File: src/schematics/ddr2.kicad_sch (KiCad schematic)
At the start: 23 parts

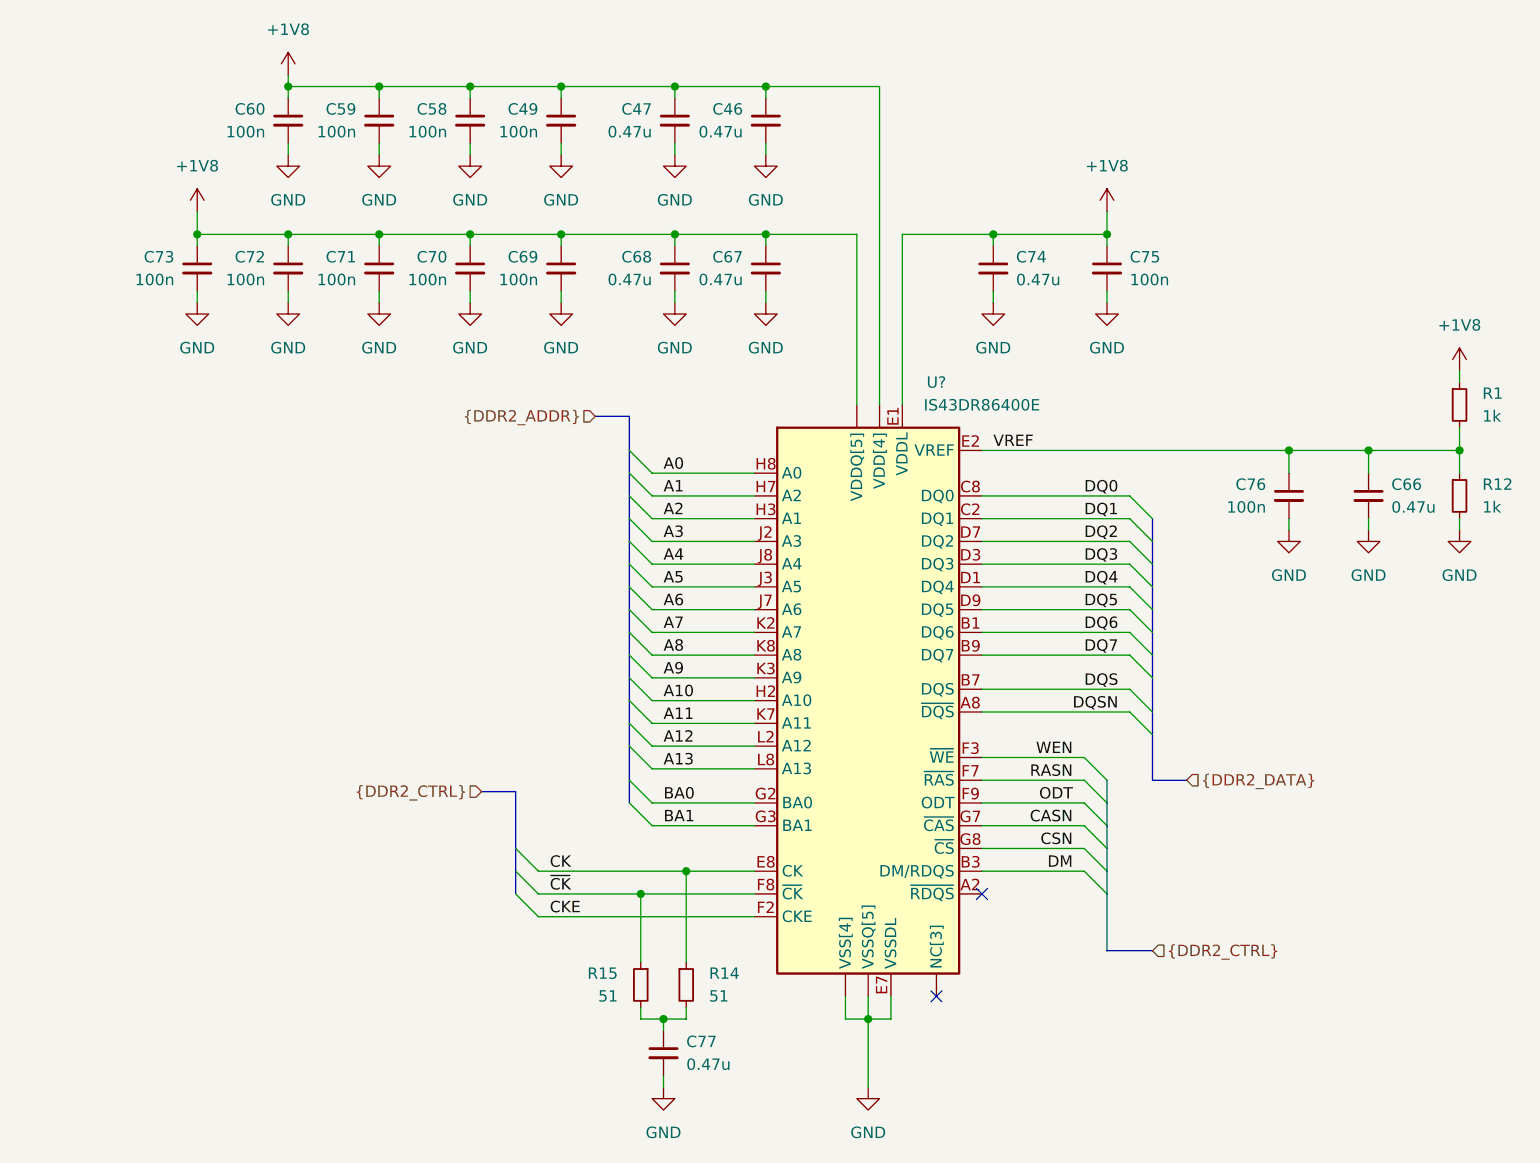
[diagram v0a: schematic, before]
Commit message: Adds the clock oscillator
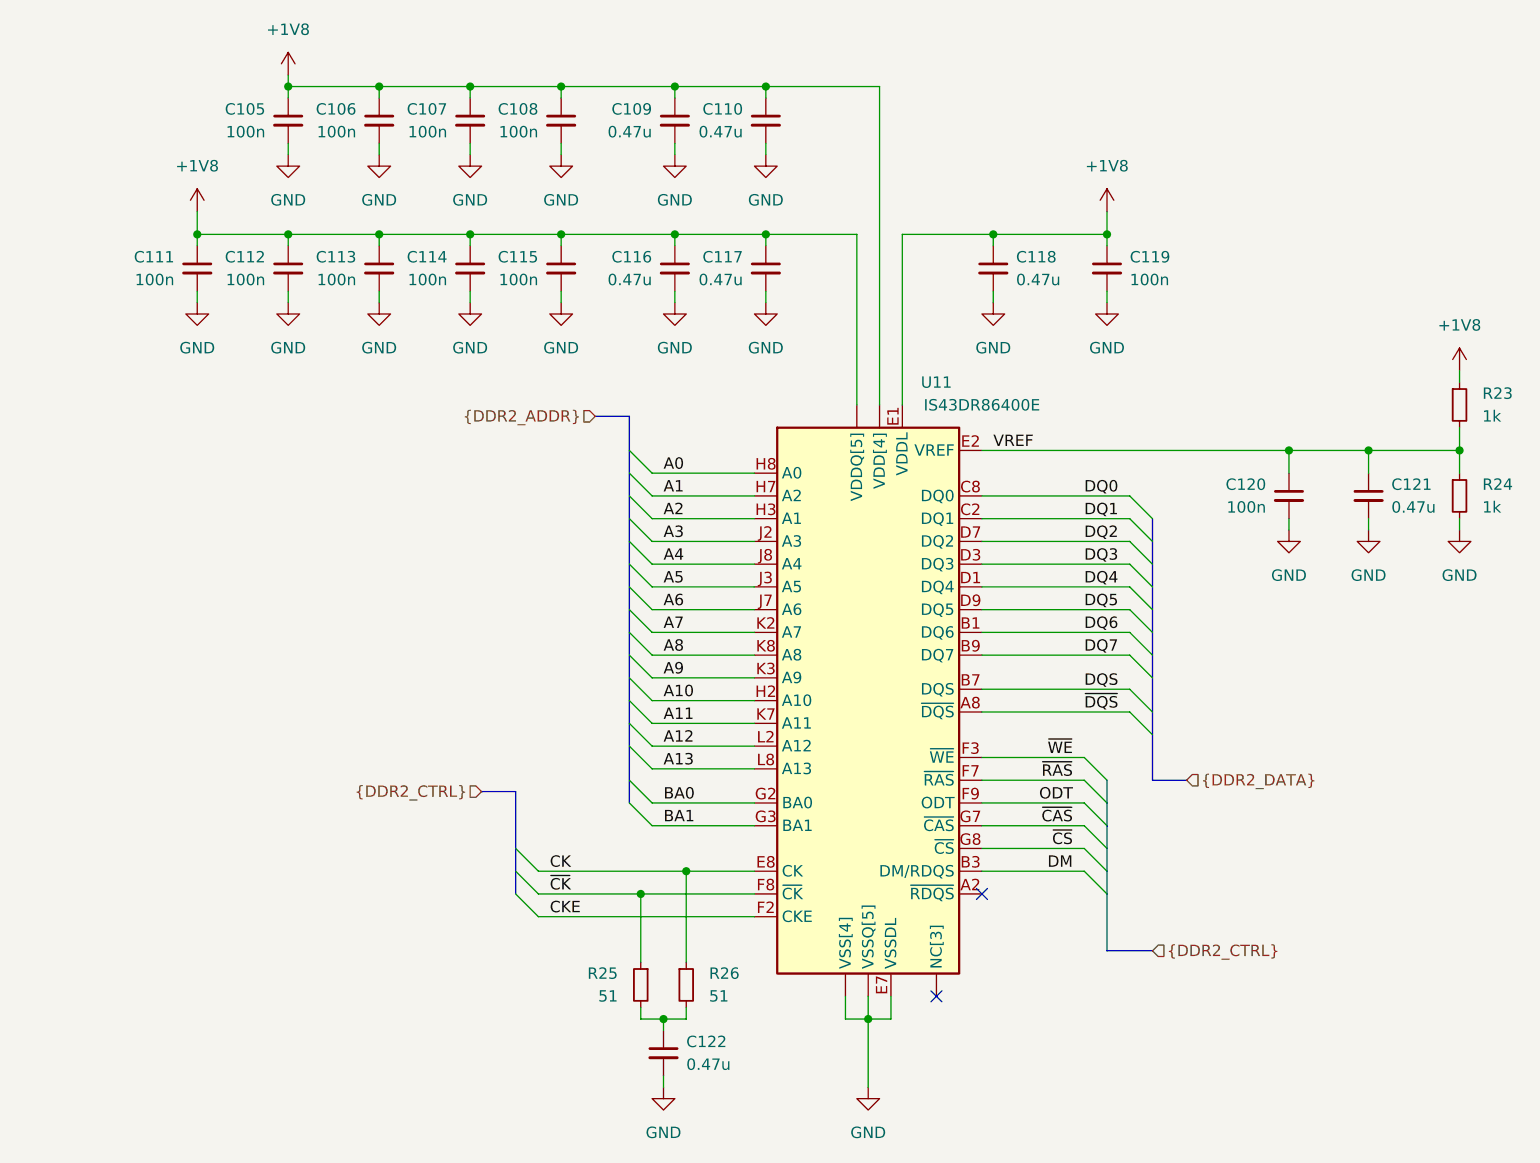
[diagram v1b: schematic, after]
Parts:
- gave numbers to parts that had none: 1
- renumbered C60 to C105, C59 to C106, C58 to C107, C49 to C108, C47 to C109, C46 to C110, C73 to C111, C72 to C112, C71 to C113, C70 to C114, C69 to C115, C68 to C116, C67 to C117, C74 to C118, C75 to C119, C76 to C120, C66 to C121, C77 to C122, R1 to R23, R12 to R24, R15 to R25, R14 to R26
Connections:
- net CASN renamed ~{CAS}
- net CSN renamed ~{CS}
- net DQSN renamed ~{DQS}
- net RASN renamed ~{RAS}
- net WEN renamed ~{WE}

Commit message: Adds bus aliases
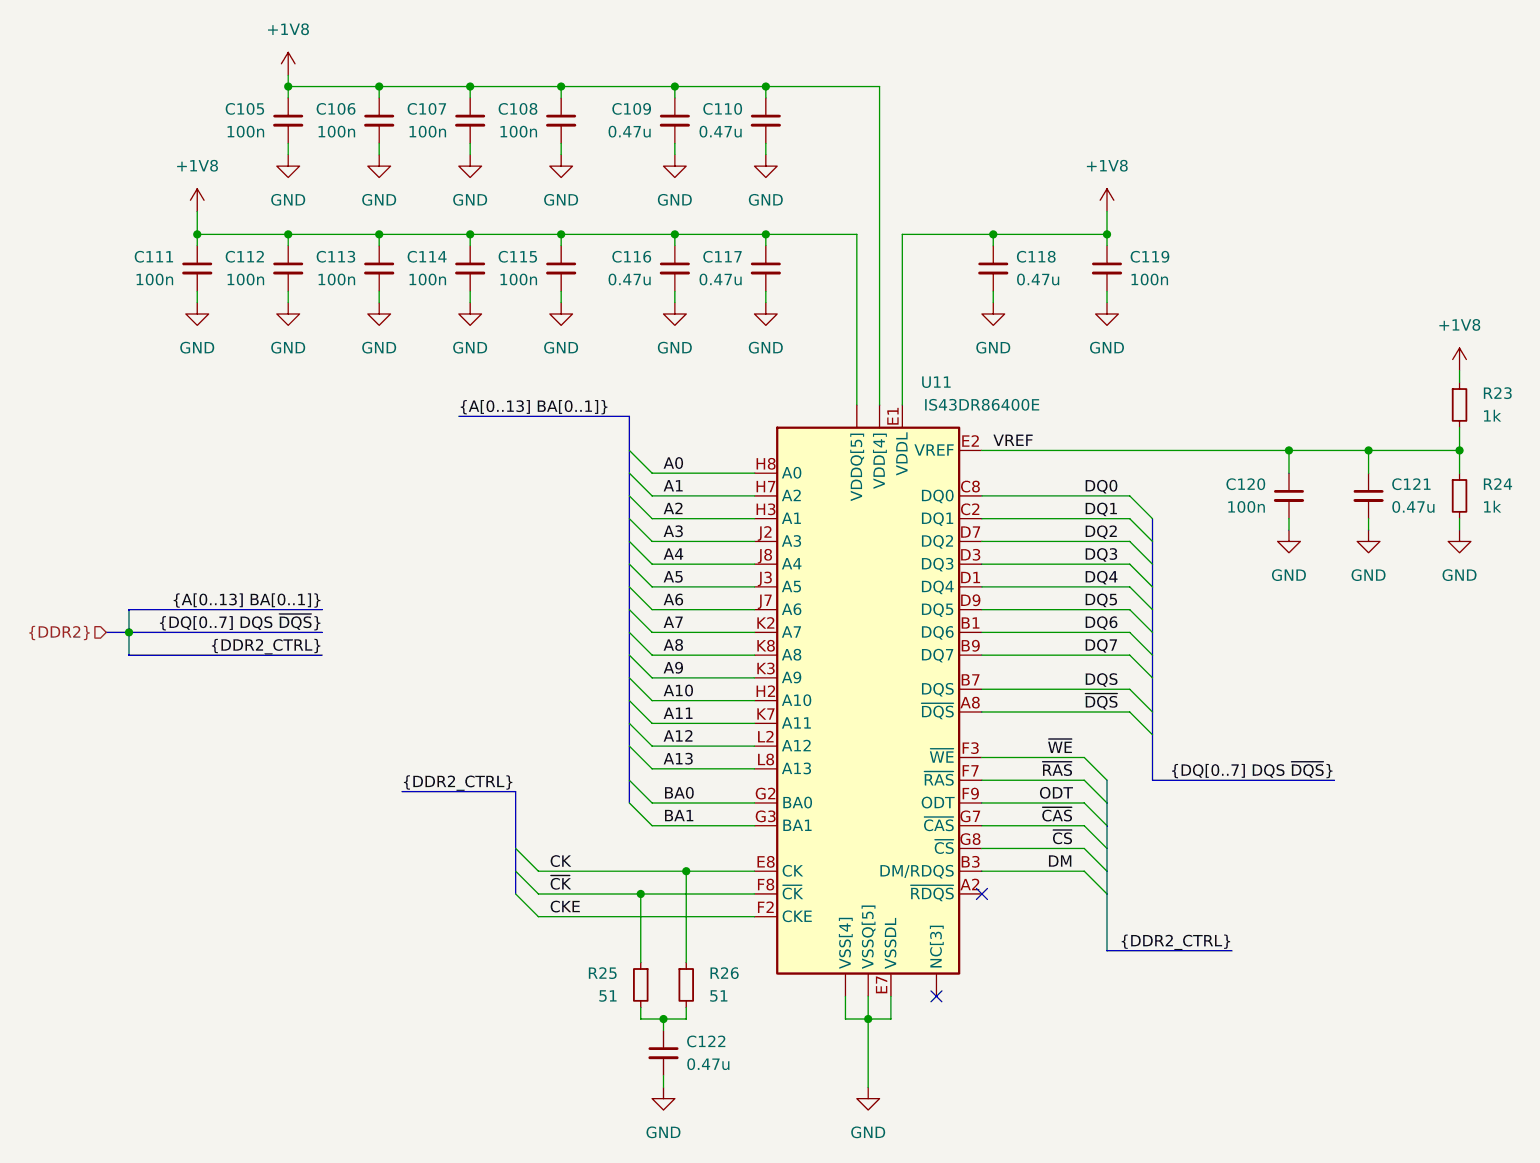
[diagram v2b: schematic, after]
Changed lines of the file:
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@@
 		(rev "${Revision}")
 		(comment 1 "${Project Title}")
-		(comment 2 "SRAM")
+		(comment 2 "DDR2")
 		(comment 3 "${Part Number}")
+	)
+	(bus_alias "DDR2"
+		(members "A[0..13]" "BA[0..1]" "DQ[0..7]" "DQS" "~{DQS}" "{DDR2_CTRL}")
+	)
+	(bus_alias "DDR2_CTRL"
+		(members "~{LB}" "~{UB}" "~{WE}" "~{OE}" "~{CE}")
 	)
 	(junction
@@
 	)
 	(junction
+		(at 67.31 92.71)
+		(diameter 0)
+		(color 0 0 0 0)
+	)
+	(junction
 		(at 129.54 119.38)
 		(diameter 0)
@@
 		)
 	)
+	(bus
+		(pts
+			(xy 104.14 68.58) (xy 123.19 68.58)
+		)
+		(stroke
+			(width 0)
+			(type default)
+		)
+	)
 	(wire
 		(pts
@@
 		)
 	)
+	(bus
+		(pts
+			(xy 67.31 92.71) (xy 88.9 92.71)
+		)
+		(stroke
+			(width 0)
+			(type default)
+		)
+	)
 	(wire
 		(pts
@@
 		)
 	)
+	(bus
+		(pts
+			(xy 97.79 110.49) (xy 110.49 110.49)
+		)
+		(stroke
+			(width 0)
+			(type default)
+		)
+	)
 	(wire
 		(pts
@@
 	(bus
 		(pts
+			(xy 67.31 92.71) (xy 67.31 95.25)
+		)
+		(stroke
+			(width 0)
+			(type default)
+		)
+	)
+	(bus
+		(pts
 			(xy 123.19 105.41) (xy 123.19 102.87)
 		)
@@
 		)
 	)
+	(bus
+		(pts
+			(xy 67.31 92.71) (xy 67.31 90.17)
+		)
+		(stroke
+			(width 0)
+			(type default)
+		)
+	)
 	(wire
 		(pts
@@
 	(bus
 		(pts
-			(xy 181.61 128.27) (xy 176.53 128.27)
-		)
-		(stroke
-			(width 0)
-			(type default)
-		)
-	)
-	(bus
-		(pts
 			(xy 176.53 114.3) (xy 176.53 111.76)
 		)
@@
 	(bus
 		(pts
+			(xy 176.53 128.27) (xy 190.5 128.27)
+		)
+		(stroke
+			(width 0)
+			(type default)
+		)
+	)
+	(bus
+		(pts
 			(xy 123.19 68.58) (xy 123.19 72.39)
 		)
@@
 		)
 	)
+	(bus
+		(pts
+			(xy 64.77 92.71) (xy 67.31 92.71)
+		)
+		(stroke
+			(width 0)
+			(type default)
+		)
+	)
 	(wire
 		(pts
@@
 		)
 	)
+	(bus
+		(pts
+			(xy 67.31 90.17) (xy 88.9 90.17)
+		)
+		(stroke
+			(width 0)
+			(type default)
+		)
+	)
 	(wire
 		(pts
@@
 	(bus
 		(pts
+			(xy 181.61 109.22) (xy 201.93 109.22)
+		)
+		(stroke
+			(width 0)
+			(type default)
+		)
+	)
+	(bus
+		(pts
 			(xy 176.53 128.27) (xy 176.53 121.92)
 		)
@@
 	(bus
 		(pts
+			(xy 88.9 95.25) (xy 67.31 95.25)
+		)
+		(stroke
+			(width 0)
+			(type default)
+		)
+	)
+	(bus
+		(pts
 			(xy 181.61 82.55) (xy 181.61 80.01)
 		)
@@
 		)
 	)
-	(bus
-		(pts
-			(xy 119.38 68.58) (xy 123.19 68.58)
-		)
-		(stroke
-			(width 0)
-			(type default)
-		)
-	)
 	(wire
 		(pts
@@
 		)
 	)
-	(bus
-		(pts
-			(xy 185.42 109.22) (xy 181.61 109.22)
-		)
-		(stroke
-			(width 0)
-			(type default)
-		)
-	)
 	(wire
 		(pts
@@
 	(bus
 		(pts
-			(xy 106.68 110.49) (xy 110.49 110.49)
-		)
-		(stroke
-			(width 0)
-			(type default)
-		)
-	)
-	(bus
-		(pts
 			(xy 123.19 109.22) (xy 123.19 105.41)
 		)
@@
 			(width 0)
 			(type default)
+		)
+	)
+	(label "{DDR2_CTRL}"
+		(at 88.9 95.25 180)
+		(fields_autoplaced yes)
+		(effects
+			(font
+				(size 1.27 1.27)
+			)
+			(justify right bottom)
 		)
 	)
@@
 		)
 	)
+	(label "{A[0..13] BA[0..1]}"
+		(at 88.9 90.17 180)
+		(fields_autoplaced yes)
+		(effects
+			(font
+				(size 1.27 1.27)
+			)
+			(justify right bottom)
+		)
+	)
 	(label "DQS"
 		(at 177.8 99.06 180)
@@
 		)
 	)
+	(label "{DDR2_CTRL}"
+		(at 190.5 128.27 180)
+		(fields_autoplaced yes)
+		(effects
+			(font
+				(size 1.27 1.27)
+			)
+			(justify right bottom)
+		)
+	)
 	(label "DM"
 		(at 172.72 119.38 180)
@@
 		)
 	)
+	(label "{DQ[0..7] DQS ~{DQS}}"
+		(at 88.9 92.71 180)
+		(fields_autoplaced yes)
+		(effects
+			(font
+				(size 1.27 1.27)
+			)
+			(justify right bottom)
+		)
+	)
 	(label "A0"
 		(at 127 74.93 0)
@@
 		)
 	)
+	(label "{DQ[0..7] DQS ~{DQS}}"
+		(at 201.93 109.22 180)
+		(fields_autoplaced yes)
+		(effects
+			(font
+				(size 1.27 1.27)
+			)
+			(justify right bottom)
+		)
+	)
 	(label "ODT"
 		(at 172.72 111.76 180)
@@
 		)
 	)
+	(label "{DDR2_CTRL}"
+		(at 97.79 110.49 0)
+		(fields_autoplaced yes)
+		(effects
+			(font
+				(size 1.27 1.27)
+			)
+			(justify left bottom)
+		)
+	)
+	(label "{A[0..13] BA[0..1]}"
+		(at 104.14 68.58 0)
+		(fields_autoplaced yes)
+		(effects
+			(font
+				(size 1.27 1.27)
+			)
+			(justify left bottom)
+		)
+	)
 	(label "A1"
 		(at 127 77.47 0)
@@
 		)
 	)
-	(hierarchical_label "{DDR2_CTRL}"
+	(hierarchical_label "{DDR2}"
 		(shape input)
-		(at 181.61 128.27 0)
-		(fields_autoplaced yes)
-		(effects
-			(font
-				(size 1.27 1.27)
-			)
-			(justify left)
-		)
-	)
-	(hierarchical_label "{DDR2_CTRL}"
-		(shape input)
-		(at 106.68 110.49 180)
+		(at 64.77 92.71 180)
 		(fields_autoplaced yes)
 		(effects
@@
 		)
 	)
-	(hierarchical_label "{DDR2_ADDR}"
-		(shape input)
-		(at 119.38 68.58 180)
-		(fields_autoplaced yes)
-		(effects
-			(font
-				(size 1.27 1.27)
-			)
-			(justify right)
-		)
-	)
-	(hierarchical_label "{DDR2_DATA}"
-		(shape input)
-		(at 185.42 109.22 0)
-		(fields_autoplaced yes)
-		(effects
-			(font
-				(size 1.27 1.27)
-			)
-			(justify left)
-		)
-	)

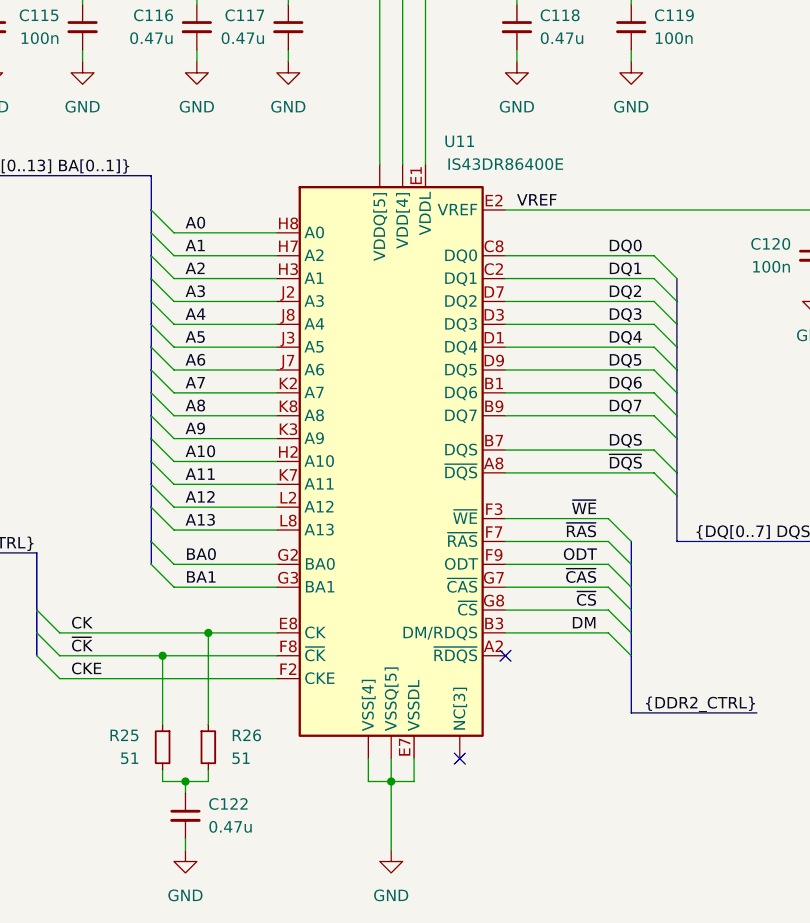
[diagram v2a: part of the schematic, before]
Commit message: Fix some ERC issues
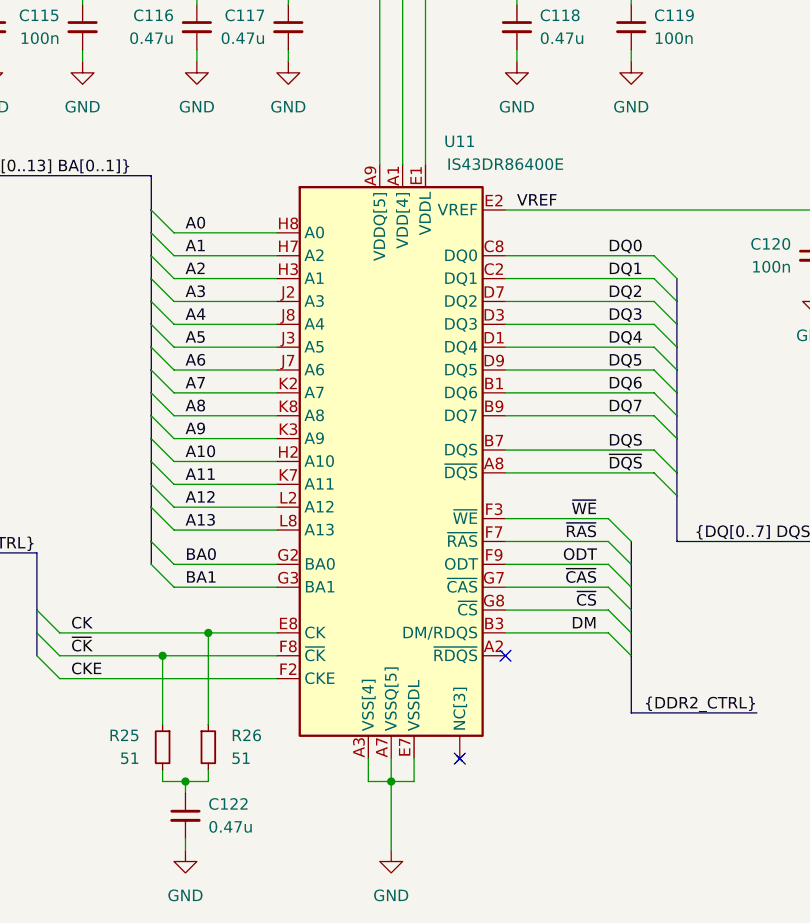
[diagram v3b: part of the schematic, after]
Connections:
- net +1V8: no longer U11. (VSS[4])
- net GND: no longer U11. (VSS[4])
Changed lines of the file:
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@@
-		(pin ""
-		)
-		(pin ""
-		)
 		(pin ""
 		)
@@
 		)
 		(pin "H2"
-		)
-		(pin ""
 		)
 		(pin "A3"
@@
 		(pin "K9"
 		)
-		(pin ""
-		)
 		(pin "B2"
